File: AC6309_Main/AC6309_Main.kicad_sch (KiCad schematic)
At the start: 13 parts, among them J1 Address Bus, J2 Data and Control, SW1 Reset, U1 HD63B09P, U2 W24257, U3 28C256, U4 74HCT00, U5 TMP68681, U6 MAX3232, Y1 7.3728 MHz

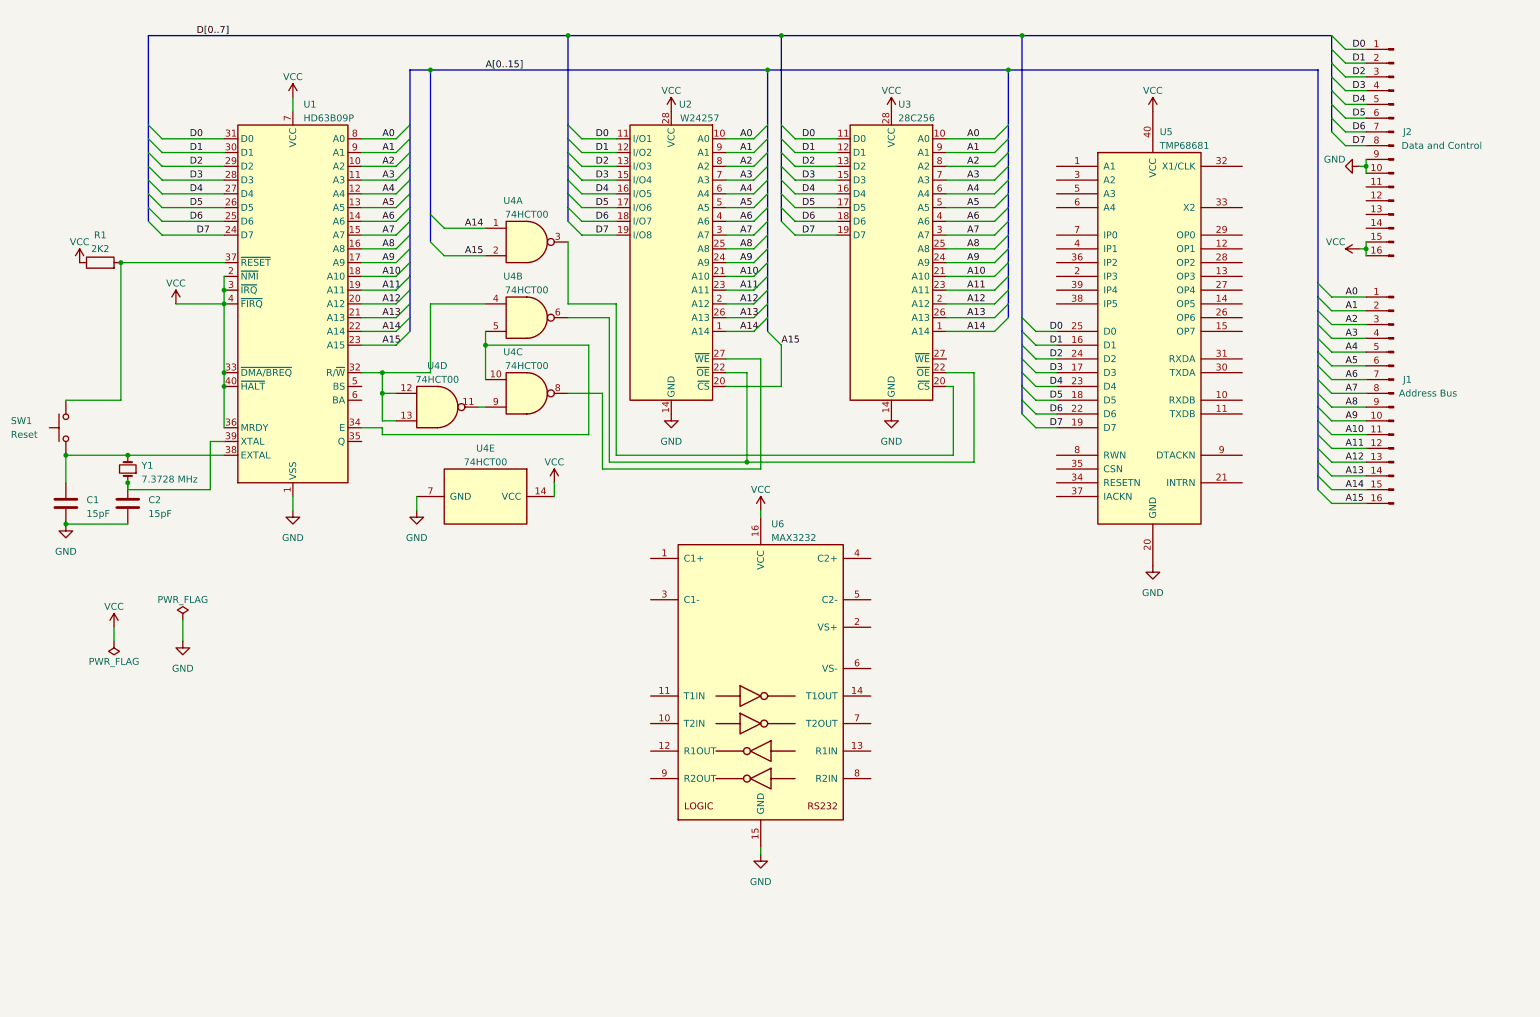
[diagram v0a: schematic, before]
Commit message: Adding 74HC138 to the address decoder
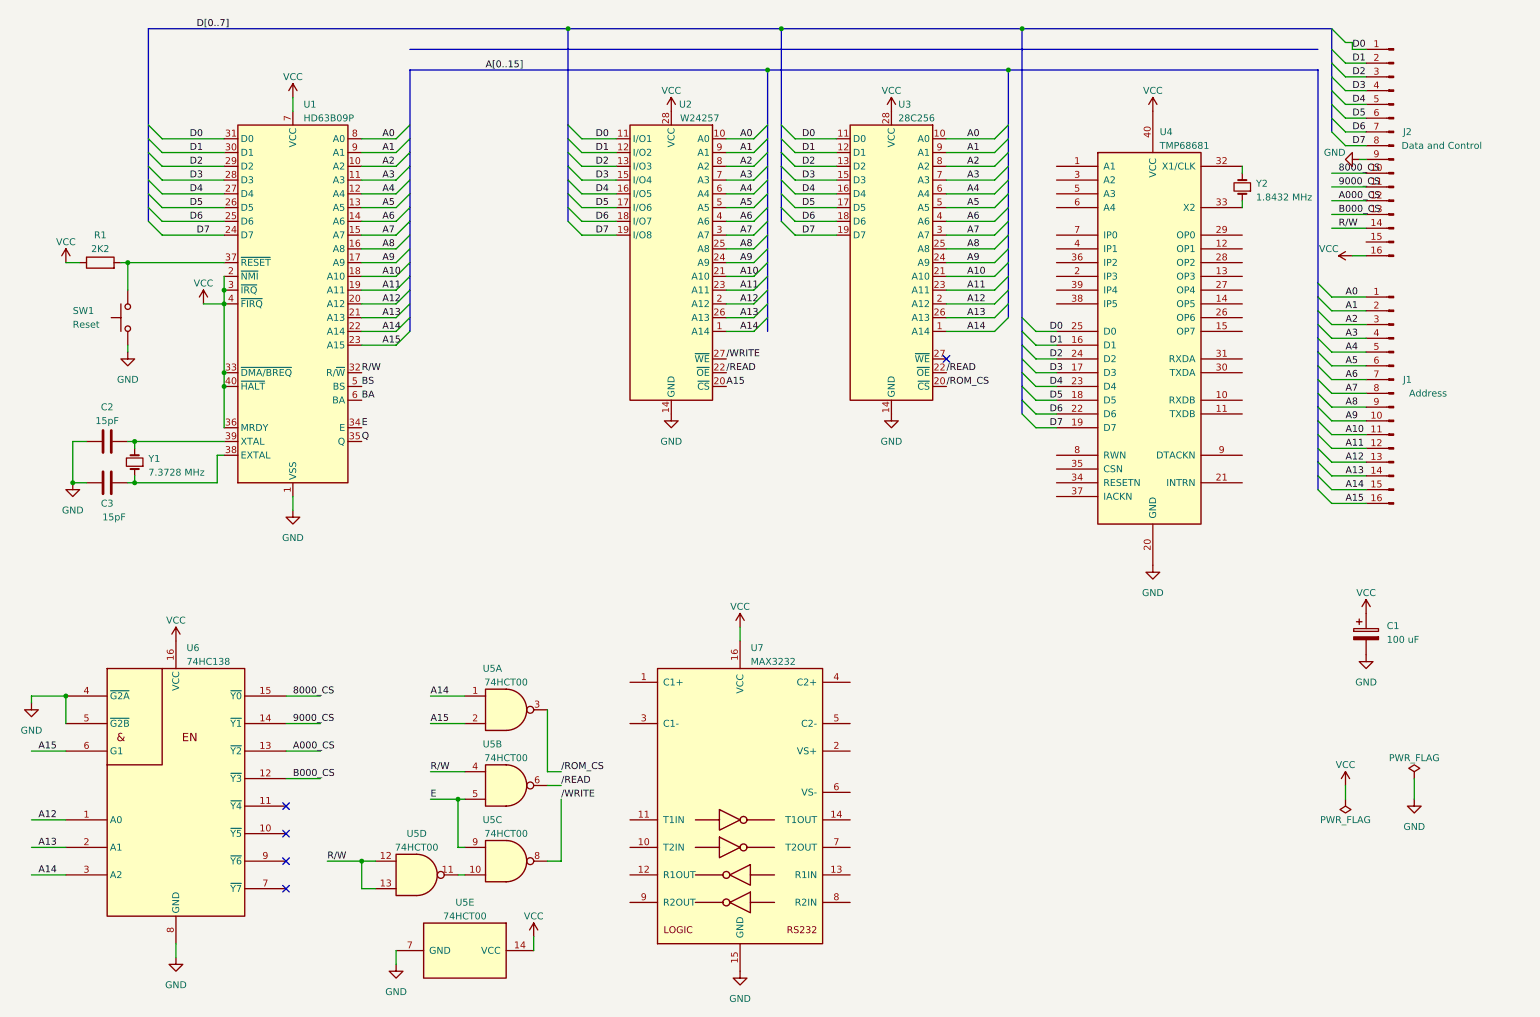
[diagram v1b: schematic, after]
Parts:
- added C1: 100 uF, Capacitor_THT:CP_Radial_D4.0mm_P2.00mm, symbol Device:C_Polarized
- added U6: 74HC138, Package_DIP:DIP-16_W7.62mm_Socket, symbol 74xx_IEEE:74LS138
- added Y2: 1.8432 MHz, Crystal:Crystal_HC49-U_Vertical, symbol Device:Crystal_Small
- C2: renamed from C1; footprint (none) -> Capacitor_THT:C_Disc_D3.0mm_W1.6mm_P2.50mm
- C3: renamed from C2; footprint (none) -> Capacitor_THT:C_Disc_D3.0mm_W1.6mm_P2.50mm
- J1: value Address Bus -> Address
- R1: footprint (none) -> Resistor_THT:R_Axial_DIN0204_L3.6mm_D1.6mm_P2.54mm_Vertical
- SW1: footprint (none) -> Button_Switch_THT:SW_TH_Tactile_Omron_B3F-10xx
- U3: footprint Package_DIP:DIP-40_W15.24mm_Socket -> Package_DIP:DIP-28_W15.24mm_Socket
- U5: renamed from U4; footprint Package_DIP:DIP-14_W7.62mm_Socket -> Package_DIP:DIP-14_W7.62mm_Socket_LongPads
- U5: renamed from U4; footprint (none) -> Package_DIP:DIP-14_W7.62mm_Socket_LongPads
- Y1: footprint (none) -> Crystal:Crystal_HC49-U_Vertical
- renumbered U5 to U4, U6 to U7
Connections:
- net A12: now also U6.1 (A0)
- net A13: now also U6.2 (A1)
- net A14: now also U6.3 (A2)
- net A15: now also U6.6 (G1)
- net GND: now also SW1.1, C1.2, U6.4 (~{G2A}), U6.5 (~{G2B}), U6.8 (GND); no longer J2.10 (Pin_10)
- net VCC: now also C1.1, U6.16 (VCC); no longer J2.15 (Pin_15)
- net /ROM_CS: now reaches U3.20 (~{CS}), U5.3
- net /READ: now reaches U2.22 (~{OE}), U3.22 (~{OE}), U5.6
- net E: now reaches U1.34 (E), U5.5
- net E: now also U5.9; no longer U5.10
- net /WRITE: now reaches U2.27 (~{WE}), U5.8
- net at U5.11: now also U5.10; no longer U5.9
- net at C2.1, Y1.2: now also U1.39 (XTAL); no longer SW1.1, U1.38 (EXTAL)
- net 9000_CS: now reaches J2.11 (Pin_11)
- net 9000_CS: now also U6.14 (~{Y1})
- net A000_CS: now reaches J2.12 (Pin_12)
- net A000_CS: now also U6.13 (~{Y2})
- net B000_CS: now reaches J2.13 (Pin_13)
- net B000_CS: now also U6.12 (~{Y3})
- net R/W: now reaches J2.14 (Pin_14)
- net R/W: now also U1.32 (R/~{W}), U5.12, U5.13, U5.4
- net at C3.1, Y1.1: now also U1.38 (EXTAL); no longer U1.39 (XTAL)
- net at U4.32 (X1/CLK): now also Y2.2
- net at U4.33 (X2): now also Y2.1
- net Q: now reaches U1.35 (Q)
- net BS: now reaches U1.5 (BS)
- net BA: now reaches U1.6 (BA)
- new net 8000_CS: J2.10 (Pin_10), U6.15 (~{Y0})
- no-connect marks 0 -> 5
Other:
- moved on the sheet: C2, C3, SW1, U5A, U5B, U5C, U5D, U5E, U7, Y1

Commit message: Added resistor networks. Updated PCB layout. Added temporary freeroute traces.
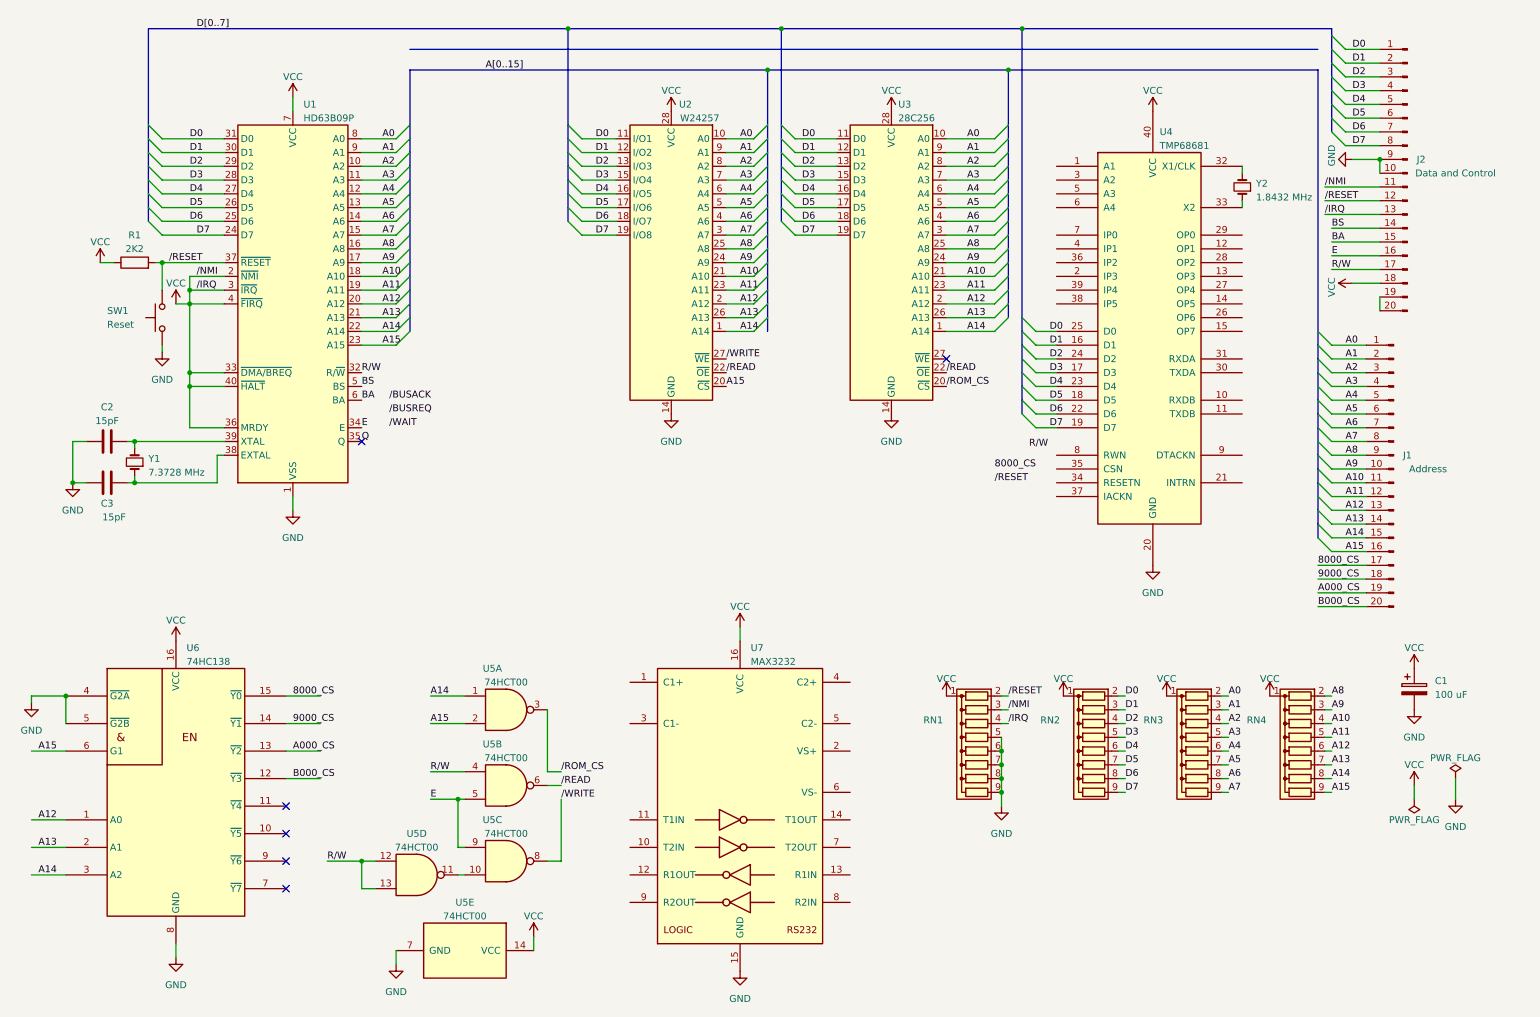
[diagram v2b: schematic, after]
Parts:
- added RN1, RN2, RN3, RN4: R_Network08, Resistor_THT:R_Array_SIP9, symbol Device:R_Network08
- J1, J2: symbol Connector:Conn_01x16_Pin -> Connector:Conn_01x20_Pin
- U5: footprint Package_DIP:DIP-14_W7.62mm_Socket_LongPads -> Package_DIP:DIP-14_W7.62mm_Socket
- U7: footprint Package_DIP:DIP-16_W7.62mm_Socket_LongPads -> Package_DIP:DIP-16_W7.62mm_Socket
- Y1, Y2: footprint Crystal:Crystal_HC49-U_Vertical -> Crystal:Crystal_HC49-4H_Vertical
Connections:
- net 8000_CS: now also J1.17 (Pin_17); no longer J2.10 (Pin_10)
- net 9000_CS: now also J1.18 (Pin_18); no longer J2.11 (Pin_11)
- net A0: now also RN3.2 (R1)
- net A000_CS: now also J1.19 (Pin_19); no longer J2.12 (Pin_12)
- net A1: now also RN3.3 (R2)
- net A10: now also RN4.4 (R3)
- net A11: now also RN4.5 (R4)
- net A12: now also RN4.6 (R5)
- net A13: now also RN4.7 (R6)
- net A14: now also RN4.8 (R7)
- net A15: now also RN4.9 (R8)
- net A2: now also RN3.4 (R3)
- net A3: now also RN3.5 (R4)
- net A4: now also RN3.6 (R5)
- net A5: now also RN3.7 (R6)
- net A6: now also RN3.8 (R7)
- net A7: now also RN3.9 (R8)
- net A8: now also RN4.2 (R1)
- net A9: now also RN4.3 (R2)
- net B000_CS: now also J1.20 (Pin_20); no longer J2.13 (Pin_13)
- net BA: now also J2.15 (Pin_15)
- net BS: now also J2.14 (Pin_14)
- net D0: now also RN2.2 (R1)
- net D1: now also RN2.3 (R2)
- net D2: now also RN2.4 (R3)
- net D3: now also RN2.5 (R4)
- net D4: now also RN2.6 (R5)
- net D5: now also RN2.7 (R6)
- net D6: now also RN2.8 (R7)
- net D7: now also RN2.9 (R8)
- net E: now also J2.16 (Pin_16)
- net GND: now also J2.10 (Pin_10), RN1.5 (R4), RN1.6 (R5), RN1.7 (R6), RN1.8 (R7), RN1.9 (R8)
- net R/W: now also J2.17 (Pin_17); no longer J2.14 (Pin_14)
- net VCC: now also J2.11 (Pin_11), J2.13 (Pin_13), J2.18 (Pin_18), RN1.1 (common), RN1.3 (R2), RN1.4 (R3), RN2.1 (common), RN3.1 (common), RN4.1 (common); no longer J2.16 (Pin_16)
- net /RESET: now reaches R1.2, SW1.2, U1.37 (~{RESET})
- net /RESET: now also J2.12 (Pin_12), RN1.2 (R1)
- new net: J2.19 (Pin_19), J2.20 (Pin_20)
- no-connect marks 5 -> 6
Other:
- moved on the sheet: C1, R1, SW1

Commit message: Replaced UART. Updates on Readme .
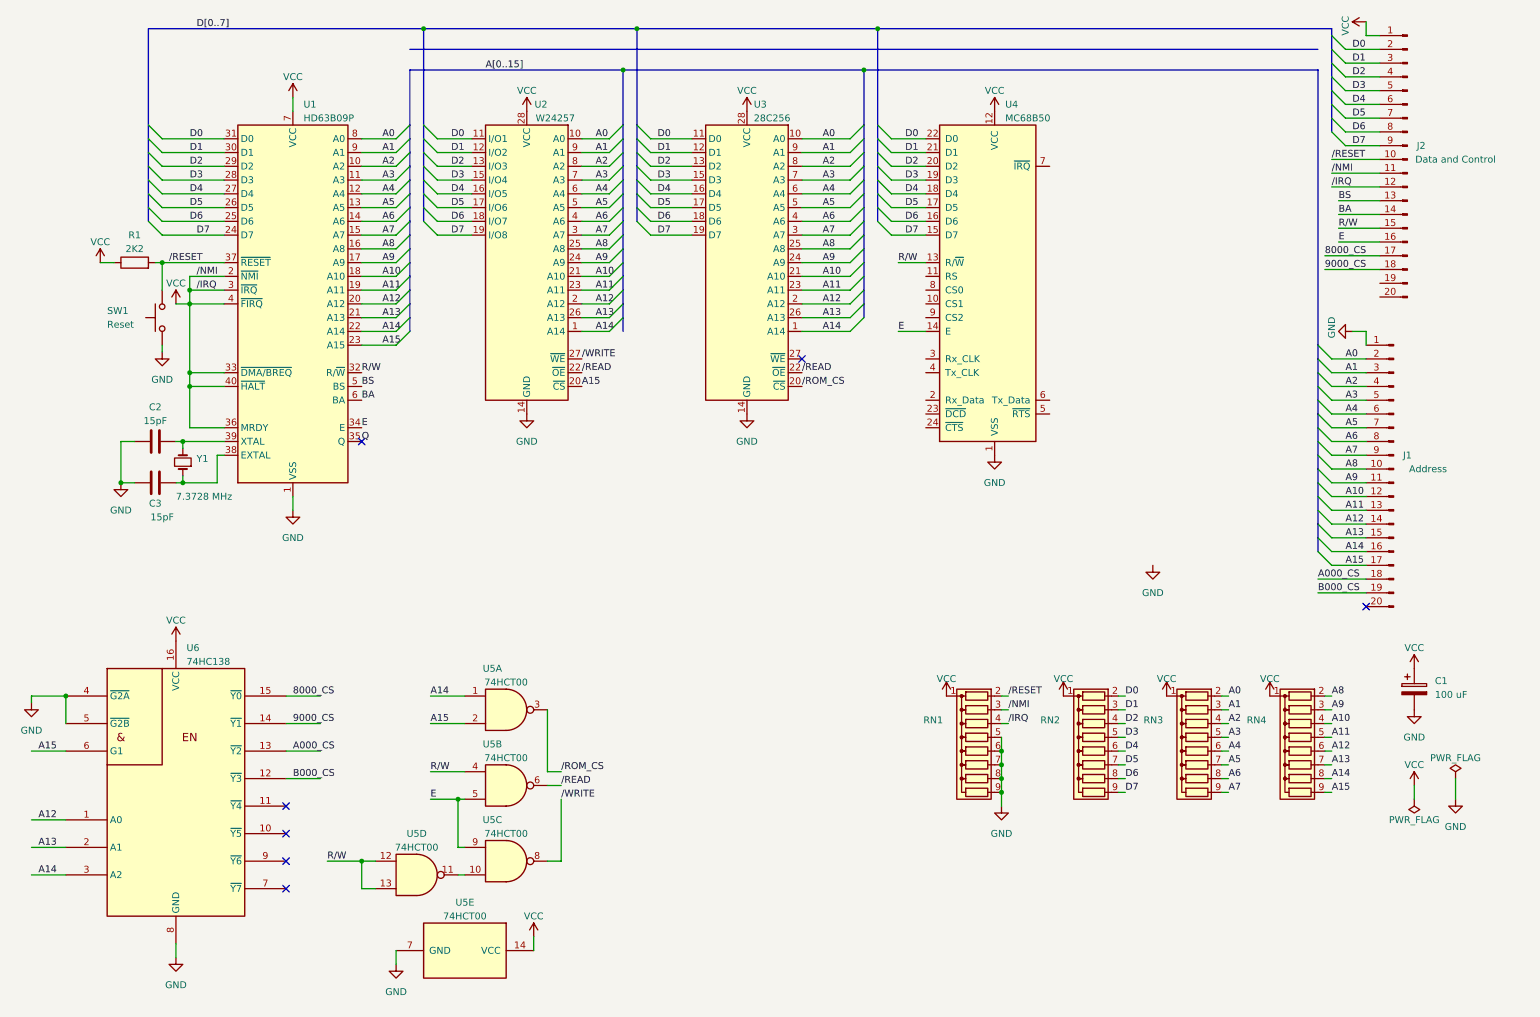
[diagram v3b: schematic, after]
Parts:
- removed U4: TMP68681, Package_DIP:DIP-40_W15.24mm_Socket, symbol TMP68681P:TMP68681P
- removed U7: MAX3232, Package_DIP:DIP-16_W7.62mm_Socket, symbol Interface_UART:MAX3232
- removed Y2: 1.8432 MHz, Crystal:Crystal_HC49-4H_Vertical, symbol Device:Crystal_Small
- added U4: MC68B50, Package_DIP:DIP-24_W15.24mm_Socket, symbol Interface_UART:MC68B50
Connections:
- net 8000_CS: now also J2.17 (Pin_17); no longer J1.17 (Pin_17)
- net 9000_CS: now also J2.18 (Pin_18); no longer J1.18 (Pin_18)
- net A0: now also J1.2 (Pin_2); no longer J1.1 (Pin_1)
- net A000_CS: now also J1.18 (Pin_18); no longer J1.19 (Pin_19)
- net A1: now also J1.3 (Pin_3); no longer J1.2 (Pin_2)
- net A10: now also J1.12 (Pin_12); no longer J1.11 (Pin_11)
- net A11: now also J1.13 (Pin_13); no longer J1.12 (Pin_12)
- net A12: now also J1.14 (Pin_14); no longer J1.13 (Pin_13)
- net A13: now also J1.15 (Pin_15); no longer J1.14 (Pin_14)
- net A14: now also J1.16 (Pin_16); no longer J1.15 (Pin_15)
- net A15: now also J1.17 (Pin_17); no longer J1.16 (Pin_16)
- net A2: now also J1.4 (Pin_4); no longer J1.3 (Pin_3)
- net A3: now also J1.5 (Pin_5); no longer J1.4 (Pin_4)
- net A4: now also J1.6 (Pin_6); no longer J1.5 (Pin_5)
- net A5: now also J1.7 (Pin_7); no longer J1.6 (Pin_6)
- net A6: now also J1.8 (Pin_8); no longer J1.7 (Pin_7)
- net A7: now also J1.9 (Pin_9); no longer J1.8 (Pin_8)
- net A8: now also J1.10 (Pin_10); no longer J1.9 (Pin_9)
- net A9: now also J1.11 (Pin_11); no longer J1.10 (Pin_10)
- net B000_CS: now also J1.19 (Pin_19); no longer J1.20 (Pin_20)
- net BA: now also J2.14 (Pin_14); no longer J2.15 (Pin_15)
- net BS: now also J2.13 (Pin_13); no longer J2.14 (Pin_14)
- net D0: now also J2.2 (Pin_2), U4.22 (D0); no longer J2.1 (Pin_1)
- net D1: now also J2.3 (Pin_3), U4.21 (D1); no longer J2.2 (Pin_2)
- net D2: now also J2.4 (Pin_4), U4.20 (D2); no longer J2.3 (Pin_3)
- net D3: now also J2.5 (Pin_5), U4.19 (D3); no longer J2.4 (Pin_4)
- net D4: now also J2.6 (Pin_6), U4.18 (D4); no longer J2.5 (Pin_5)
- net D5: now also J2.7 (Pin_7), U4.17 (D5); no longer J2.6 (Pin_6)
- net D6: now also J2.8 (Pin_8), U4.16 (D6); no longer J2.7 (Pin_7)
- net D7: now also J2.9 (Pin_9), U4.15 (D7); no longer J2.8 (Pin_8)
- net E: now also U4.14 (E)
- net GND: now also J1.1 (Pin_1), U4.1 (VSS); no longer J2.10 (Pin_10), J2.9 (Pin_9)
- net R/W: now also J2.15 (Pin_15), U4.13 (R/~{W}); no longer J2.17 (Pin_17)
- net VCC: now also J2.1 (Pin_1), J2.12 (Pin_12), U4.12 (VCC); no longer J2.13 (Pin_13), J2.18 (Pin_18)
- net /RESET: now also J2.10 (Pin_10); no longer J2.12 (Pin_12)
- net at J2.19 (Pin_19): no longer J2.20 (Pin_20)
- no-connect marks 6 -> 7
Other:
- moved on the sheet: C2, C3, J2, U2, U3, Y1

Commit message: Schematics revision 1, Digital file, etc.
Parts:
- added J3: FTDI Header, Connector_PinHeader_2.54mm:PinHeader_1x06_P2.54mm_Vertical, symbol Connector:Conn_01x06_Pin
- J1, J2: footprint Connector_PinHeader_2.00mm:PinHeader_1x20_P2.00mm_Vertical -> Connector_PinHeader_2.54mm:PinHeader_1x20_P2.54mm_Vertical
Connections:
- net A0: now also U4.11 (RS)
- net A13: now also U4.10 (CS1)
- net A14: now also U4.9 (CS2)
- net A15: now also U4.8 (CS0)
- net E: now also U4.3 (Rx_CLK), U4.4 (Tx_CLK)
- net GND: now also U4.23 (~{DCD}), J3.6 (Pin_6); no longer RN1.5 (R4), RN1.6 (R5), RN1.7 (R6), RN1.8 (R7)
- net VCC: now also J3.4 (Pin_4); no longer J2.11 (Pin_11), J2.12 (Pin_12), RN1.3 (R2), RN1.4 (R3), U1.2 (~{NMI}), U1.3 (~{IRQ}), U1.33 (~{DMA/BREQ}), U1.36 (MRDY), U1.4 (~{FIRQ}), U1.40 (~{HALT})
- net C000_CS: now reaches U6.11 (~{Y4})
- net at U4.2 (Rx_Data): now also J3.3 (Pin_3)
- net at U4.24 (~{CTS}): now also U4.5 (~{RTS})
- net at U4.6 (Tx_Data): now also J3.2 (Pin_2)
- net /IRQ: now reaches U4.7 (~{IRQ})
- net /IRQ: now also J2.12 (Pin_12), RN1.4 (R3), U1.3 (~{IRQ})
- net BA: no longer names the net of U1.6 (BA)
- net BA: no longer J2.14 (Pin_14)
- net BS: no longer names the net of U1.5 (BS)
- net BS: no longer J2.13 (Pin_13)
- new net MRDY: RN1.8 (R7), U1.36 (MRDY)
- new net /DMABREQ: RN1.6 (R5), U1.33 (~{DMA/BREQ})
- new net /FIRQ: J2.13 (Pin_13), RN1.5 (R4), U1.4 (~{FIRQ})
- new net /HALT: J2.14 (Pin_14), RN1.7 (R6), U1.40 (~{HALT})
- new net /NMI: J2.11 (Pin_11), RN1.3 (R2), U1.2 (~{NMI})
- no-connect marks 7 -> 12
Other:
- note added: "CTS"
- note added: "GND"
- note added: "RTS"
- note added: "RX"
- note added: "TX"
- note added: "VCC"
- moved on the sheet: C2, C3, R1, RN1, SW1, Y1

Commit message: KiCad sync
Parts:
- added C4, C5, C6, C7, C8: 100 nF, Capacitor_THT:CP_Radial_D4.0mm_P2.00mm, symbol Device:C_Polarized
- U4: value MC68B50 -> HD63B50
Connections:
- net GND: now also C4.2, C5.2, C6.2, C7.2, C8.2
- net VCC: now also C4.1, C5.1, C6.1, C7.1, C8.1
- net A000_CS: no longer names the net of J1.18 (Pin_18)
- net A000_CS: no longer U6.13 (~{Y2})
- net C000_CS renamed C000_CS_ROM
- new net A000_CS_ACIA: U6.13 (~{Y2})
- no-connect marks 12 -> 13
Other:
- note added: "TODO: 1. Sort the connections for enabling 74138 2. Enable hardware handshake on the ACIA 3. Enable ROM switching 4. Thicker power net"
- title: AC6309 Main -> AC29 Main
